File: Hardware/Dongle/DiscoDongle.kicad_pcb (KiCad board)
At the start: 2 copper layers, 60.5 x 18.8 mm, 22 parts, among them J1 RJ45, P1 USB_B, P2 FTDI, U1 FT232RL, U2 ISL81487E

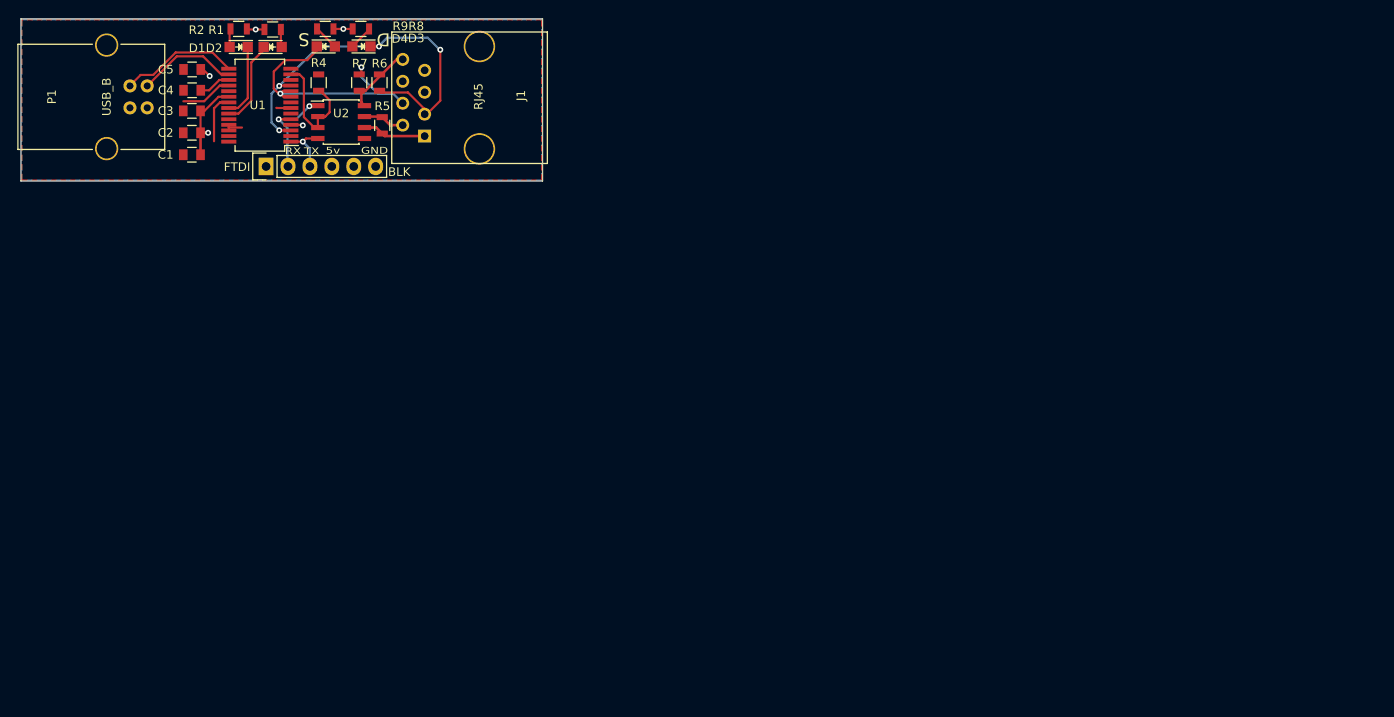
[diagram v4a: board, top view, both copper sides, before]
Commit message: DiscoDongle - Rev5 - Move components to bottom.
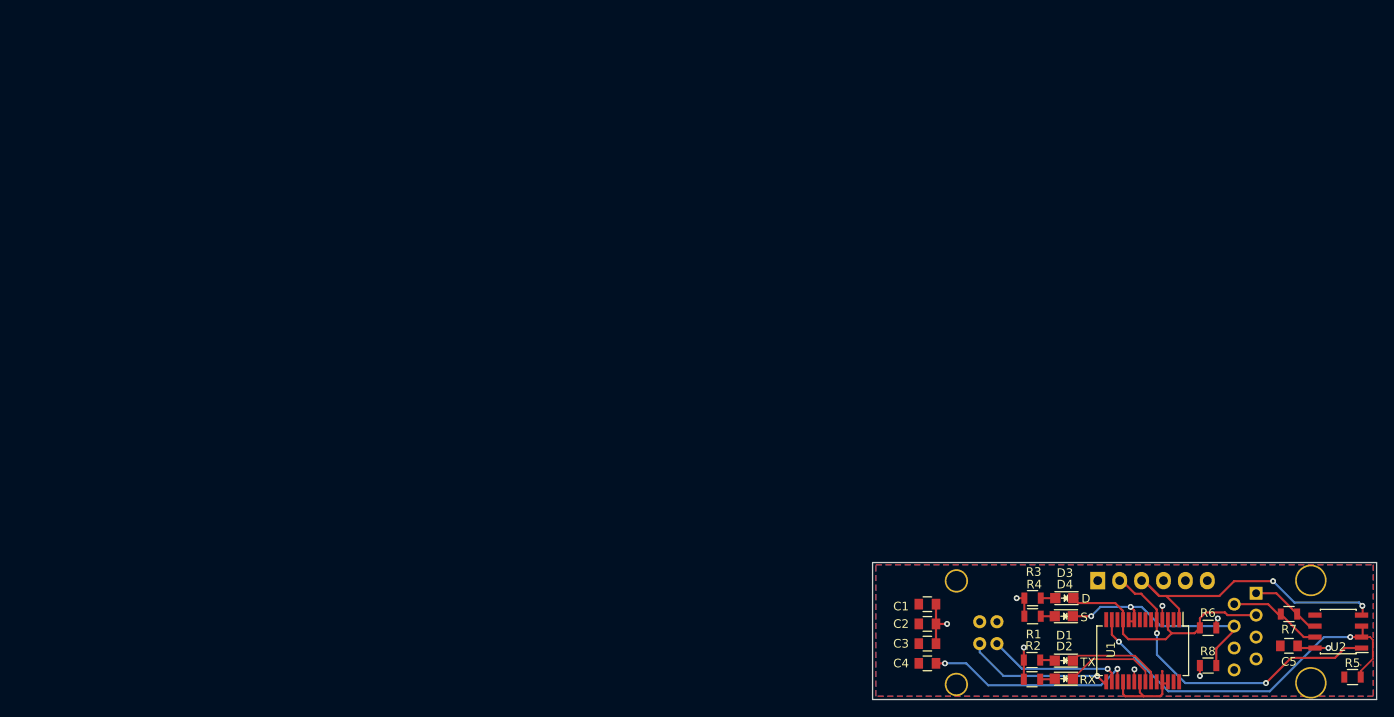
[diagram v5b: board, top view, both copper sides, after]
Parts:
- removed R9: 200, Resistors_SMD:R_0805
- added R3: 200, Resistors_SMD:R_0805, F.Cu at (156.0, 101.3)
- C5: value 0.1uF -> 100nF
- D3: value LED -> D
- D4: value LED -> S
- J1, P1, P2: moved to B.Cu
- R4: value 20k -> 200
- R5: value 120 -> 20k
- R7: value 20k -> 120
- R8: value 200 -> 20k
- moved C5 143.6 mm to (185.7, 106.8)
- moved U2 129.8 mm to (191.4, 105.2), turned to 180 degrees
- moved R5 129.4 mm to (193.0, 110.4), turned to 180 degrees
- moved R7 124.1 mm to (185.7, 103.1), turned to 0 degrees
- moved R8 122.8 mm to (176.3, 109.1)
- moved D2 120.4 mm to (159.6, 110.6)
- moved U1 120.3 mm to (168.7, 107.4), turned to 270 degrees
- moved R2 118.9 mm to (155.9, 110.7), turned to 0 degrees
- moved D1 116.0 mm to (159.6, 108.5), turned to 180 degrees
- moved P1 115.1 mm to (151.8, 104.0)
- moved R6 115.0 mm to (176.3, 104.7), turned to 180 degrees
- moved J1 114.5 mm to (188.2, 105.2), turned to 270 degrees
- moved R1 114.4 mm to (155.9, 108.5)
- moved D4 108.1 mm to (159.6, 103.4), turned to 180 degrees
- moved C4 108.0 mm to (143.8, 108.8)
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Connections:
- J1 pad 7: +5V -> Net-(J1-Pad7)
- J1 pad 8: +5V -> Net-(J1-Pad8)
- R4 pad 1: Net-(R4-Pad1) -> +5V
- R4 pad 2: GND -> Net-(D4-Pad2)
- R5 pad 1: Net-(J1-Pad2) -> Net-(R5-Pad1)
- R5 pad 2: Net-(J1-Pad1) -> GND
- R7 pad 1: +5V -> Net-(J1-Pad2)
- R7 pad 2: Signal -> Net-(J1-Pad1)
- R8 pad 2: Net-(D3-Pad2) -> Signal
- U1 pad 13: Net-(R4-Pad1) -> Net-(R5-Pad1)
- U2 pad 2: Net-(R4-Pad1) -> Net-(R5-Pad1)
- U2 pad 3: Net-(R4-Pad1) -> Net-(R5-Pad1)
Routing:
- net Net-(R5-Pad1): track 0.00 -> 43.4 mm, vias 0 -> 2
- net Net-(P2-Pad3): track 6.50 -> 35.7 mm, vias 1 -> 2
- net Net-(P2-Pad2): track 12.5 -> 38.0 mm
- net Net-(C4-Pad1): track 3.74 -> 24.4 mm, vias 0 -> 2
- net Daisy: track 47.0 -> 29.6 mm, vias 4 -> 0
- net Net-(R4-Pad1): track 16.0 -> 0.00 mm
- net Net-(J1-Pad2): track 4.85 -> 11.7 mm
- net +5V: track 26.7 -> 21.3 mm, vias 5 -> 8
- net Signal: track 33.2 -> 28.3 mm
- net GND: track 15.7 -> 11.0 mm
- net Net-(P1-Pad2): track 12.2 -> 15.9 mm, vias 0 -> 1
- net Net-(P1-Pad3): track 13.9 -> 17.3 mm, vias 0 -> 1
- net RXLED: track 8.60 -> 11.2 mm
- net TXLED: track 10.0 -> 11.9 mm
- net Net-(D4-Pad2): track 3.21 -> 1.62 mm
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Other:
- board size 60.5 x 18.8 mm -> 58.4 x 15.9 mm
- rule pad_to_mask_clearance: 0.2 -> 0
- board text added: "2016 - rev5"
- board text removed: "2016 - rev4"
- board text removed: "BLK"
- board text removed: "D"
- board text removed: "S"

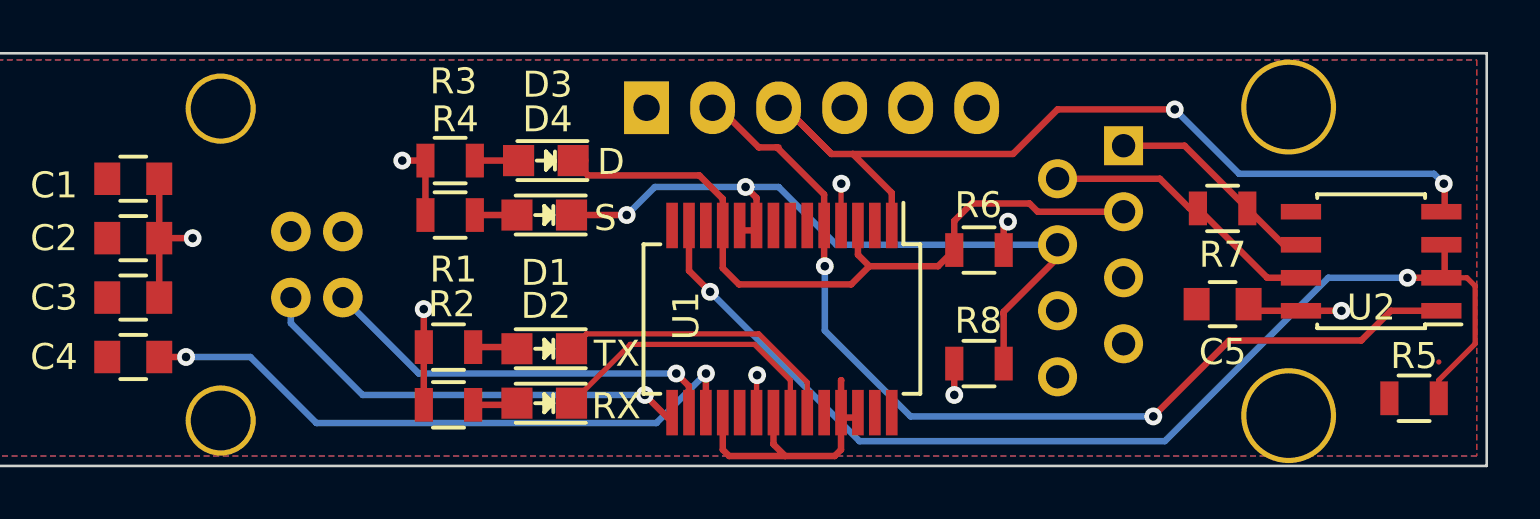
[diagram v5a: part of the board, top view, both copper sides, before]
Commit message: Simplify daily/signal connections. Remove FTDI headers.
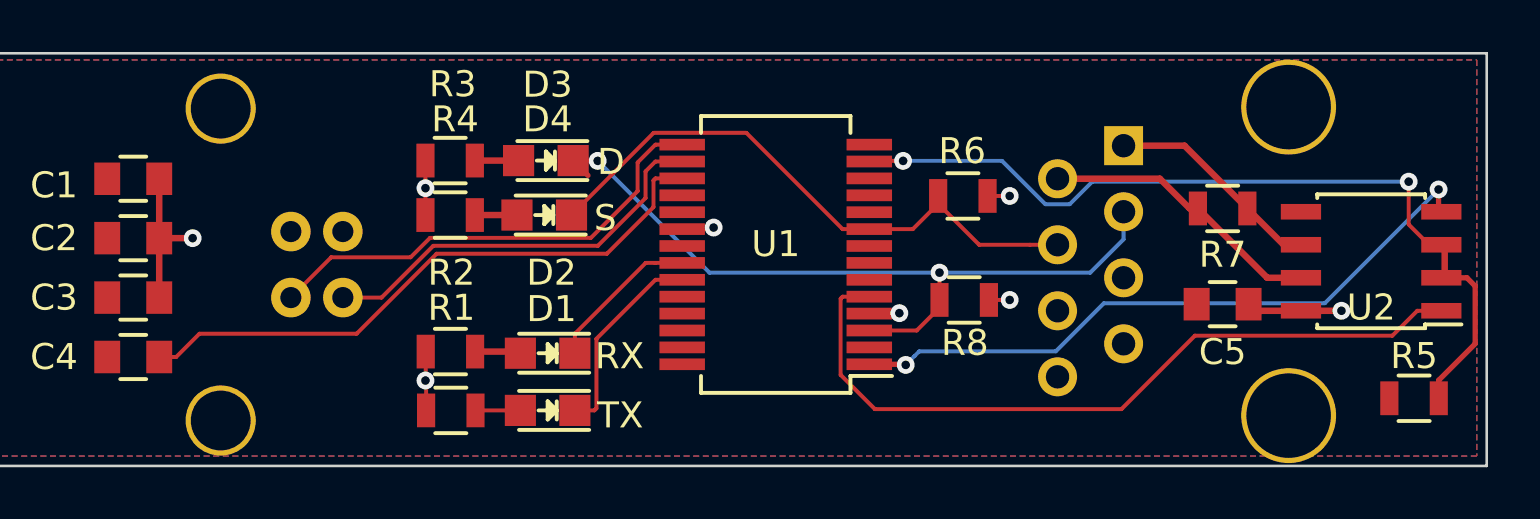
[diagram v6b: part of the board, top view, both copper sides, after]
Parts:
- removed P2: FTDI, Pin_Headers:Pin_Header_Straight_1x06
- moved R8 2.51 mm to (175.7, 106.6), turned to 180 degrees
- moved U1 2.50 mm to (168.5, 104.9), turned to 180 degrees
- moved R1 2.44 mm to (156.0, 110.9)
- moved D1 2.38 mm to (159.7, 110.9)
- moved R6 2.17 mm to (175.7, 102.6)
- moved R2 2.05 mm to (156.0, 108.6)
- moved D2 1.93 mm to (159.7, 108.7)
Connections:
- R6 pad 2: Daisy -> Signal
- R8 pad 2: Signal -> Daisy
- U1 pad 10: Signal -> Net-(U1-Pad10)
- U1 pad 11: Daisy -> Net-(U1-Pad11)
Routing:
- net GND: track 11.0 -> 0.00 mm
- net Net-(R5-Pad1): track 43.4 -> 32.5 mm
- net Net-(U1-Pad1): track 35.7 -> 25.8 mm
- net Net-(U1-Pad5): track 38.0 -> 29.3 mm, vias 2 -> 0
- net RXLED: track 11.2 -> 6.01 mm
- net Signal: track 28.3 -> 23.9 mm, vias 2 -> 0
- net TXLED: track 11.9 -> 7.78 mm
- net +5V: track 21.3 -> 17.5 mm
- net Daisy: track 29.6 -> 31.0 mm, vias 0 -> 2
- net Net-(P1-Pad3): track 17.3 -> 18.2 mm, vias 1 -> 0
- net Net-(C4-Pad1): track 24.4 -> 23.6 mm, vias 2 -> 0
- net Net-(P1-Pad2): track 15.9 -> 15.8 mm, vias 1 -> 0
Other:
- board text added: "2016 - rev6"
- board text removed: "2016 - rev5"
- board text removed: "5v"
- board text removed: "GND"
- board text removed: "RX"
- board text removed: "TX"
